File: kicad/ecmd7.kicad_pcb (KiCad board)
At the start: 4 copper layers, 120 x 90 mm, 250 parts, among them J1 PMOD_SPI_ENC, J2 PMOD_ADC_MPIO, J3 PMOD_DRV, J4 Conn_01x02_Socket, J5 Encoder, J6 12V, J7 RS422/BISS-C, J8 5V, Q1 IRFS3806, Q10 BSC098N10NS5, Q11 MMBT3904, Q12 MMBT3904, Q2 IRFS3806, Q3 IRFS3806, Q4 IRFS3806, Q5 IRFS3806, Q6 IRFS3806, Q7 BSC098N10NS5, Q8 BSC098N10NS5, Q9 BSC098N10NS5, U1 TMC6200-TA, U10 FIN1002M5X, U11 FIN1002M5X, U12 FIN1002M5X, U13 ADM3490ExR, U14 LM5118MH, U15 74LVC1G139, U16 MB85RS1MT, U17 TMP122AIDBVR, U2 MCP33151-05T-E/MN, U3 LM5118MH, U4 MCP33151-05T-E/MN, U5 MCP33151-05T-E/MN, U6 TLV71318PDBV, U7 MCP33151-05T-E/MN, U9 LT1616ES6#TRPBF

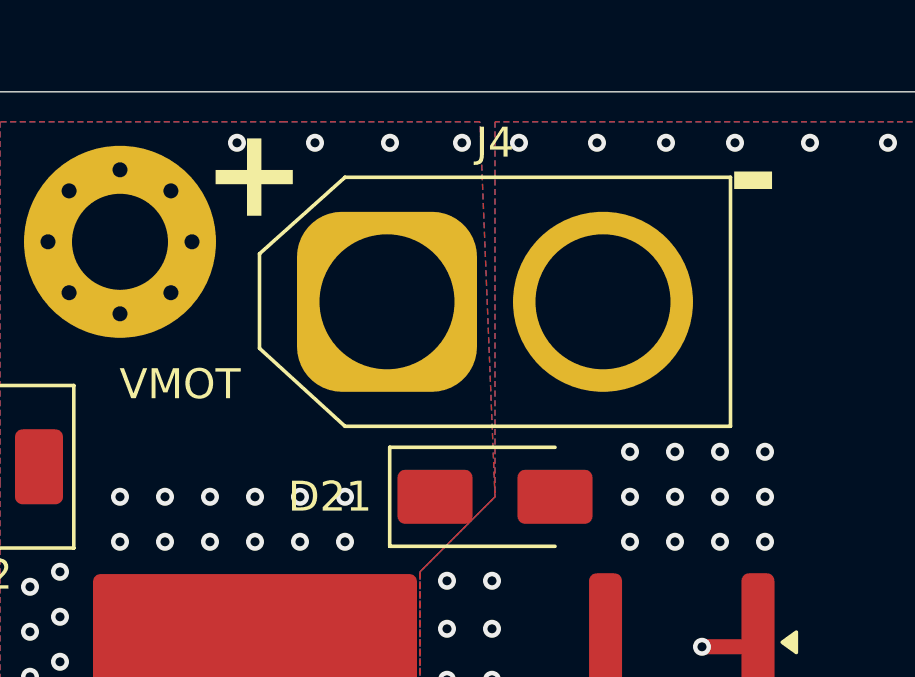
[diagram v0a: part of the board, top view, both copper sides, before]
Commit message: Fix power connector polarity
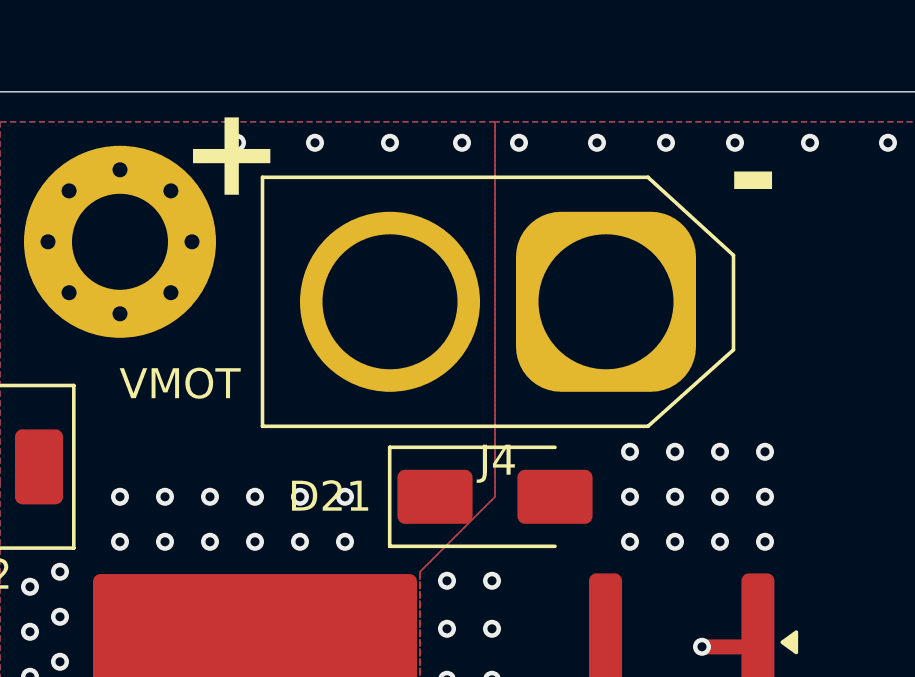
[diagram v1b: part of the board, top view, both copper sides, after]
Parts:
- moved J4 7.30 mm to (154.7, 47.0), turned to 180 degrees
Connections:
- net /ADC.MOSI0 renamed /ADC.MISO0
- net /ADC.MOSI1 renamed /ADC.MISO1
- net /ADC.MOSI2 renamed /ADC.MISO2
- net /ADC.MOSI3 renamed /ADC.MISO3
- J4 pad 1: VMot -> GNDMOT
- J4 pad 2: GNDMOT -> VMot
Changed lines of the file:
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@@
 	(net 64 "Net-(U2-AIN+)")
 	(net 65 "Net-(U4-AIN+)")
-	(net 66 "/ADC.MOSI3")
+	(net 66 "/ADC.MISO3")
 	(net 67 "Net-(U5-AIN+)")
 	(net 68 "Net-(U2-SDI)")
@@
 	(net 91 "/ENC_Z")
 	(net 92 "/ENC_A")
-	(net 93 "/ADC.MOSI2")
+	(net 93 "/ADC.MISO2")
 	(net 94 "/ADC.~{CS}")
-	(net 95 "/ADC.MOSI1")
+	(net 95 "/ADC.MISO1")
 	(net 96 "/RS422_RX")
-	(net 97 "/ADC.MOSI0")
+	(net 97 "/ADC.MISO0")
 	(net 98 "/VL")
 	(net 99 "/UH")
@@
 			(size 0.8128 0.254)
 			(layers "F.Cu" "F.Mask" "F.Paste")
-			(net 93 "/ADC.MOSI2")
+			(net 93 "/ADC.MISO2")
 			(pinfunction "SDO")
 			(pintype "output")
@@
 	(footprint "Connector_AMASS:AMASS_XT60-M_1x02_P7.20mm_Vertical"
 		(layer "F.Cu")
-		(at 147.4 47)
+		(at 154.7 47 180)
 		(descr "AMASS female XT60, through hole, vertical, https://www.tme.eu/Document/2d152ced3b7a446066e6c419d84bb460/XT60%20SPEC.pdf")
 		(tags "XT60 female vertical")
@@
 		)
 		(property "Datasheet" "~"
-			(at 0 0 0)
+			(at 0 0 180)
 			(unlocked yes)
 			(layer "F.Fab")
@@
 		)
 		(property "Description" "Generic connector, single row, 01x02, script generated"
-			(at 0 0 0)
+			(at 0 0 180)
 			(unlocked yes)
 			(layer "F.Fab")
@@
 		)
 		(property "Sim.Type" ""
-			(at 0 0 0)
+			(at 0 0 180)
 			(unlocked yes)
 			(layer "F.Fab")
@@
 		(attr through_hole)
 		(fp_line
-			(start -4.25 -1.6)
-			(end -4.25 1.55)
+			(start 11.45 4.15)
+			(end 11.45 -4.15)
 			(stroke
 				(width 0.12)
@@
 		)
 		(fp_line
-			(start -4.25 1.55)
-			(end -1.4 4.15)
+			(start 11.45 -4.15)
+			(end -1.4 -4.15)
 			(stroke
 				(width 0.12)
@@
 		)
 		(fp_line
-			(start -1.4 -4.15)
-			(end -4.25 -1.6)
+			(start -1.4 4.15)
+			(end 11.45 4.15)
 			(stroke
 				(width 0.12)
@@
 		)
 		(fp_line
-			(start -1.4 4.15)
-			(end 11.45 4.15)
+			(start -1.4 -4.15)
+			(end -4.25 -1.6)
 			(stroke
 				(width 0.12)
@@
 		)
 		(fp_line
-			(start 11.45 -4.15)
-			(end -1.4 -4.15)
+			(start -4.25 1.55)
+			(end -1.4 4.15)
 			(stroke
 				(width 0.12)
@@
 		)
 		(fp_line
-			(start 11.45 4.15)
-			(end 11.45 -4.15)
+			(start -4.25 -1.6)
+			(end -4.25 1.55)
 			(stroke
 				(width 0.12)
@@
 		)
 		(fp_line
-			(start -4.65 -1.85)
-			(end -1.6 -4.6)
+			(start 11.85 4.6)
+			(end -1.6 4.6)
 			(stroke
 				(width 0.05)
@@
 		)
 		(fp_line
-			(start -4.65 1.85)
-			(end -4.65 -1.85)
+			(start 11.85 -4.6)
+			(end 11.85 4.6)
 			(stroke
 				(width 0.05)
@@
 		)
 		(fp_line
-			(start -1.6 -4.6)
-			(end 11.85 -4.6)
+			(start -1.6 4.6)
+			(end -4.65 1.85)
 			(stroke
 				(width 0.05)
@@
 		)
 		(fp_line
-			(start -1.6 4.6)
-			(end -4.65 1.85)
+			(start -1.6 -4.6)
+			(end 11.85 -4.6)
 			(stroke
 				(width 0.05)
@@
 		)
 		(fp_line
-			(start 11.85 -4.6)
-			(end 11.85 4.6)
+			(start -4.65 1.85)
+			(end -4.65 -1.85)
 			(stroke
 				(width 0.05)
@@
 		)
 		(fp_line
-			(start 11.85 4.6)
-			(end -1.6 4.6)
+			(start -4.65 -1.85)
+			(end -1.6 -4.6)
 			(stroke
 				(width 0.05)
@@
 		)
 		(fp_line
-			(start -4.15 -1.55)
-			(end -4.15 1.55)
+			(start 11.35 4.05)
+			(end 11.35 -4.05)
 			(stroke
 				(width 0.12)
@@
 		)
 		(fp_line
-			(start -4.15 1.55)
-			(end -1.4 4.05)
+			(start 11.35 -4.05)
+			(end -1.4 -4.05)
 			(stroke
 				(width 0.12)
@@
 		)
 		(fp_line
-			(start -1.4 -4.05)
-			(end -4.15 -1.55)
+			(start -1.4 4.05)
+			(end 11.35 4.05)
 			(stroke
 				(width 0.12)
@@
 		)
 		(fp_line
-			(start -1.4 4.05)
-			(end 11.35 4.05)
+			(start -1.4 -4.05)
+			(end -4.15 -1.55)
 			(stroke
 				(width 0.12)
@@
 		)
 		(fp_line
-			(start 11.35 -4.05)
-			(end -1.4 -4.05)
+			(start -4.15 1.55)
+			(end -1.4 4.05)
 			(stroke
 				(width 0.12)
@@
 		)
 		(fp_line
-			(start 11.35 4.05)
-			(end 11.35 -4.05)
+			(start -4.15 -1.55)
+			(end -4.15 1.55)
 			(stroke
 				(width 0.12)
@@
 		)
 		(pad "1" thru_hole roundrect
-			(at 0 0)
+			(at 0 0 180)
 			(size 6 6)
 			(drill 4.5)
@@
 			(remove_unused_layers no)
 			(roundrect_rratio 0.25)
-			(net 35 "VMot")
+			(net 147 "GNDMOT")
 			(pinfunction "Pin_1")
 			(pintype "passive")
 		)
 		(pad "2" thru_hole circle
-			(at 7.2 0)
+			(at 7.2 0 180)
 			(size 6 6)
 			(drill 4.5)
 			(layers "*.Cu" "*.Mask")
 			(remove_unused_layers no)
-			(net 147 "GNDMOT")
+			(net 35 "VMot")
 			(pinfunction "Pin_2")
 			(pintype "passive")
@@
 			(size 0.8128 0.254)
 			(layers "F.Cu" "F.Mask" "F.Paste")
-			(net 97 "/ADC.MOSI0")
+			(net 97 "/ADC.MISO0")
 			(pinfunction "SDO")
 			(pintype "output")
@@
 			(size 0.8128 0.254)
 			(layers "F.Cu" "F.Mask" "F.Paste")
-			(net 66 "/ADC.MOSI3")
+			(net 66 "/ADC.MISO3")
 			(pinfunction "SDO")
 			(pintype "output")
@@
 			(layers "*.Cu" "*.Mask")
 			(remove_unused_layers no)
-			(net 93 "/ADC.MOSI2")
+			(net 93 "/ADC.MISO2")
 			(pinfunction "Pin_7")
 			(pintype "passive")
@@
 			(layers "*.Cu" "*.Mask")
 			(remove_unused_layers no)
-			(net 66 "/ADC.MOSI3")
+			(net 66 "/ADC.MISO3")
 			(pinfunction "Pin_8")
 			(pintype "passive")
@@
 			(layers "*.Cu" "*.Mask")
 			(remove_unused_layers no)
-			(net 97 "/ADC.MOSI0")
+			(net 97 "/ADC.MISO0")
 			(pinfunction "Pin_9")
 			(pintype "passive")
@@
 			(layers "*.Cu" "*.Mask")
 			(remove_unused_layers no)
-			(net 95 "/ADC.MOSI1")
+			(net 95 "/ADC.MISO1")
 			(pinfunction "Pin_10")
 			(pintype "passive")
@@
 			(size 0.8128 0.254)
 			(layers "F.Cu" "F.Mask" "F.Paste")
-			(net 95 "/ADC.MOSI1")
+			(net 95 "/ADC.MISO1")
 			(pinfunction "SDO")
 			(pintype "output")
@@
 	)
 	(gr_text "+"
-		(at 141.25 44.5 0)
+		(at 140.5 43.8 0)
 		(layer "F.SilkS")
 		(effects
@@
 		(min_thickness 0.25)
 		(filled_areas_thickness no)
-		(fill
+		(fill yes
 			(thermal_gap 0.2)
 			(thermal_bridge_width 0.8)
@@
 		(min_thickness 0.25)
 		(filled_areas_thickness no)
-		(fill
+		(fill yes
 			(thermal_gap 0.2)
 			(thermal_bridge_width 0.8)
@@
 		(min_thickness 0.25)
 		(filled_areas_thickness no)
-		(fill
+		(fill yes
 			(thermal_gap 0.4)
 			(thermal_bridge_width 0.8)
@@
 		(min_thickness 0.25)
 		(filled_areas_thickness no)
-		(fill
+		(fill yes
 			(thermal_gap 0.5)
 			(thermal_bridge_width 0.5)
@@
 		(min_thickness 0.25)
 		(filled_areas_thickness no)
-		(fill
+		(fill yes
 			(thermal_gap 0.4)
 			(thermal_bridge_width 0.8)
@@
 		(min_thickness 0.25)
 		(filled_areas_thickness no)
-		(fill
+		(fill yes
 			(thermal_gap 0.4)
 			(thermal_bridge_width 0.8)
@@
 		(min_thickness 0.25)
 		(filled_areas_thickness no)
-		(fill
+		(fill yes
 			(thermal_gap 0.4)
 			(thermal_bridge_width 0.8)
@@
 		(min_thickness 0.25)
 		(filled_areas_thickness no)
-		(fill
+		(fill yes
 			(thermal_gap 0.5)
 			(thermal_bridge_width 0.5)
@@
 		(min_thickness 0.25)
 		(filled_areas_thickness no)
-		(fill
+		(fill yes
 			(thermal_gap 0.5)
 			(thermal_bridge_width 0.5)
@@
 		(min_thickness 0.25)
 		(filled_areas_thickness no)
-		(fill
+		(fill yes
 			(thermal_gap 0.4)
 			(thermal_bridge_width 0.8)
@@
 		(min_thickness 0.25)
 		(filled_areas_thickness no)
-		(fill
+		(fill yes
 			(thermal_gap 0.5)
 			(thermal_bridge_width 0.5)
@@
 		(min_thickness 0.25)
 		(filled_areas_thickness no)
-		(fill
+		(fill yes
 			(thermal_gap 0.5)
 			(thermal_bridge_width 0.5)
@@
 		(min_thickness 0.25)
 		(filled_areas_thickness no)
-		(fill
+		(fill yes
 			(thermal_gap 0.4)
 			(thermal_bridge_width 0.8)
@@
 		(min_thickness 0.25)
 		(filled_areas_thickness no)
-		(fill
+		(fill yes
 			(thermal_gap 0.5)
 			(thermal_bridge_width 0.5)
@@
 		(min_thickness 0.25)
 		(filled_areas_thickness no)
-		(fill
+		(fill yes
 			(thermal_gap 0.5)
 			(thermal_bridge_width 0.5)
@@
 			(pts
 				(xy 144 41) (xy 134.5 41) (xy 134.5 53) (xy 134.5 106.5) (xy 148.5 106.5) (xy 148.5 56) (xy 151 53.5)
-				(xy 150.5 41)
+				(xy 151 41)
 			)
 		)
@@
 		(min_thickness 0.25)
 		(filled_areas_thickness no)
-		(fill
+		(fill yes
 			(thermal_gap 0.5)
 			(thermal_bridge_width 0.5)
@@
 		(min_thickness 0.25)
 		(filled_areas_thickness no)
-		(fill
+		(fill yes
 			(thermal_gap 0.4)
 			(thermal_bridge_width 0.8)
@@
 		(min_thickness 0.25)
 		(filled_areas_thickness no)
-		(fill
+		(fill yes
 			(thermal_gap 0.2)
 			(thermal_bridge_width 0.8)
@@
 		(min_thickness 0.25)
 		(filled_areas_thickness no)
-		(fill
+		(fill yes
 			(thermal_gap 0.2)
 			(thermal_bridge_width 0.8)
@@
 		(min_thickness 0.25)
 		(filled_areas_thickness no)
-		(fill
+		(fill yes
 			(thermal_gap 0.2)
 			(thermal_bridge_width 0.8)
@@
 		(min_thickness 0.25)
 		(filled_areas_thickness no)
-		(fill
+		(fill yes
 			(thermal_gap 0.2)
 			(thermal_bridge_width 0.8)
@@
 		(min_thickness 0.25)
 		(filled_areas_thickness no)
-		(fill
+		(fill yes
 			(thermal_gap 0.2)
 			(thermal_bridge_width 0.8)
